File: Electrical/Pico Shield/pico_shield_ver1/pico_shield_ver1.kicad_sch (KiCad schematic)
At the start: 54 parts, among them J1 644752-2, J10 B2B-PH-K-S_LF__SN_, J11 B2B-PH-K-S_LF__SN_, J12 B2B-PH-K-S_LF__SN_, J13 B2B-PH-K-S_LF__SN_, J14 B2B-PH-K-S_LF__SN_, J2 Step_connector, J3 B5B-XH-A_LF__SN_, J4 644752-2, J5 Step_connector, J6 B5B-XH-A_LF__SN_, J7 B2B-PH-K-S_LF__SN_, J8 B2B-PH-K-S_LF__SN_, J9 B2B-PH-K-S_LF__SN_, U1 XC6230A001QR-G, U2 Si1442DH, U3 ULN2003A, U4 ULN2003A, U5 pico_shield, U6 CD4051B, U7 LM358

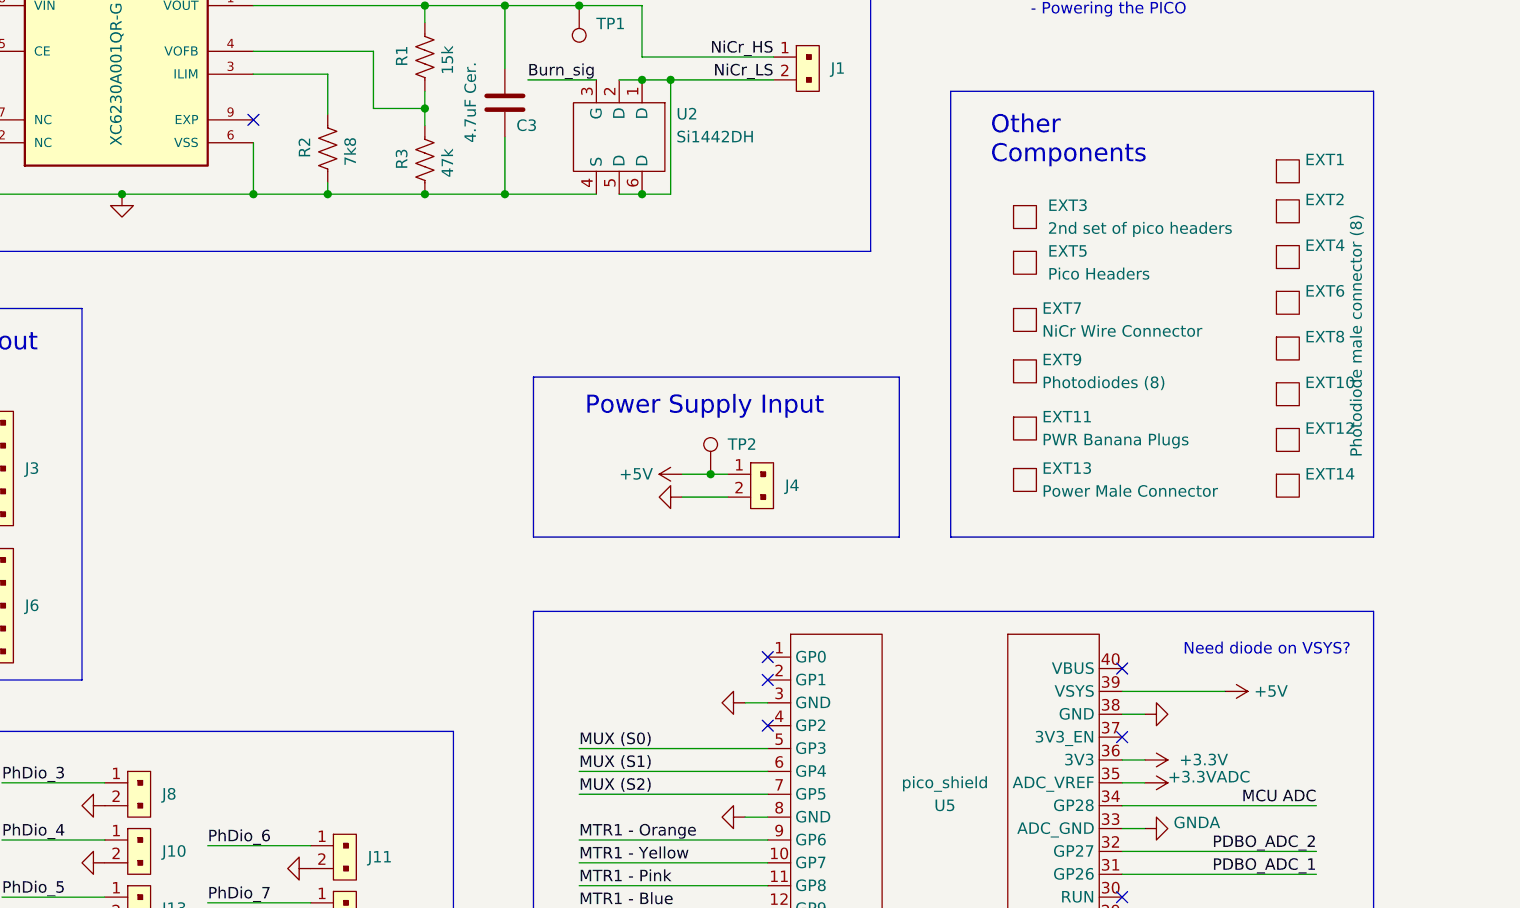
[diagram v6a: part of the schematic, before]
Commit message: Added Custom Symbols and README
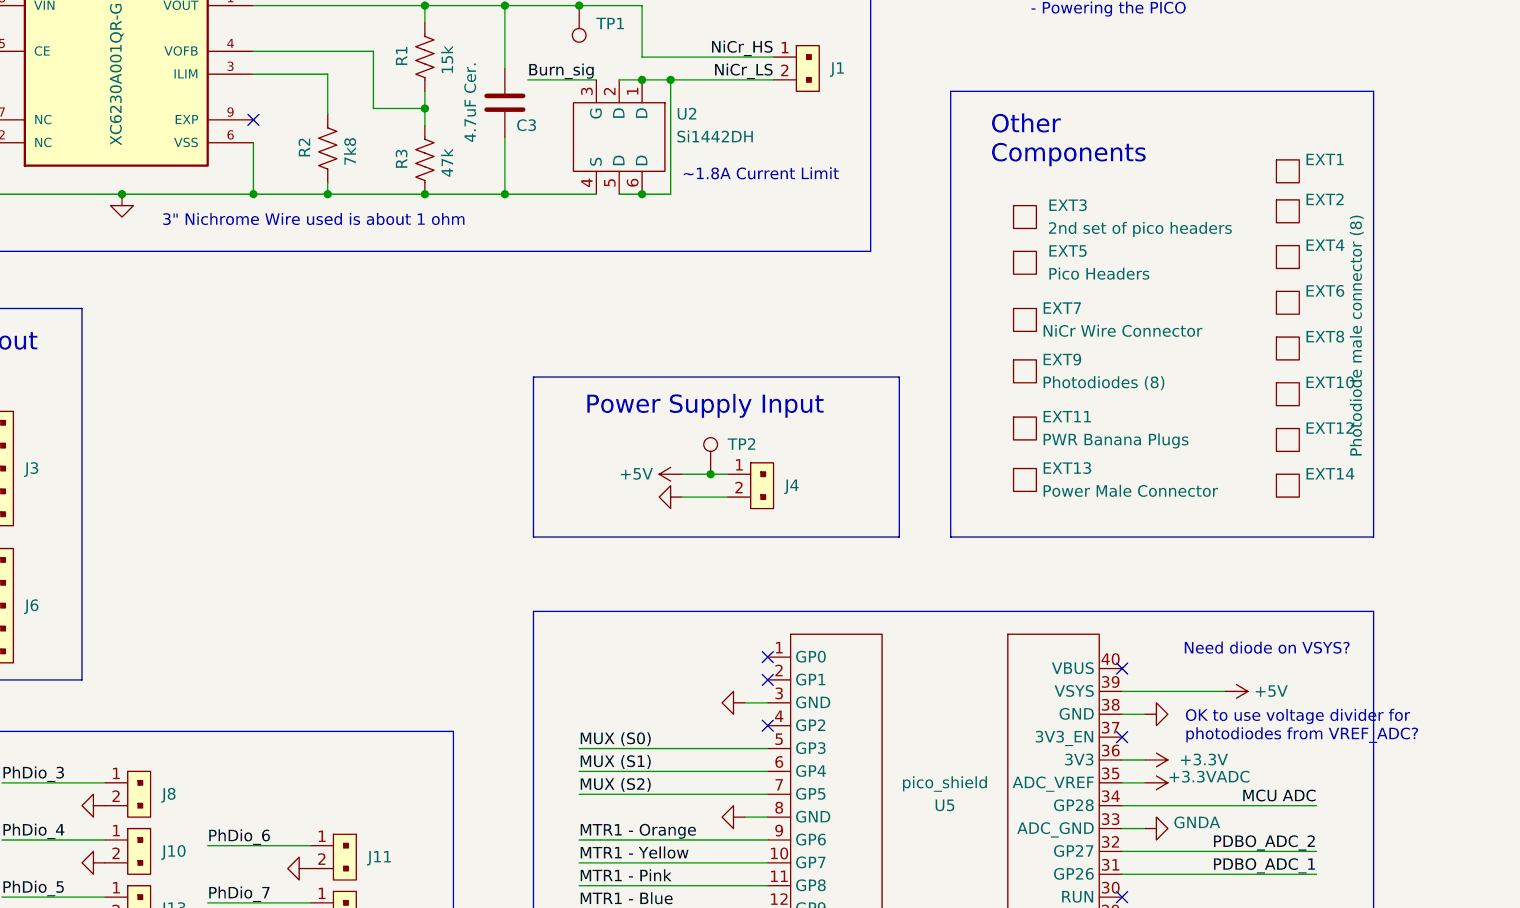
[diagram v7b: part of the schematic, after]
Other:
- note added: "3" Nichrome Wire used is about 1 ohm"
- note added: "OK to use voltage divider for photodiodes from VREF_ADC?"
- note added: "~1.8A Current Limit"
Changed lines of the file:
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@@
     (effects (font (size 2 2)) (justify left bottom))
+  )
+  (text "~1.8A Current Limit" (at 197.485 49.53 0)
+    (effects (font (size 1.27 1.27)) (justify left bottom))
+  )
+  (text "3\" Nichrome Wire used is about 1 ohm" (at 139.7 54.61 0)
+    (effects (font (size 1.27 1.27)) (justify left bottom))
   )
   (text "NiChrome Wire Burner\n" (at 179.07 26.67 0)
@@
   (text "Need diode on VSYS?" (at 271.78 102.235 180)
     (effects (font (size 1.27 1.27)) (justify right bottom))
+  )
+  (text "OK to use voltage divider for \nphotodiodes from VREF_ADC?"
+    (at 253.365 111.76 0)
+    (effects (font (size 1.27 1.27)) (justify left bottom))
   )
   (text "Step Motor Drivers" (at 53.975 33.02 0)
@@
       (effects (font (size 1.524 1.524)) (justify left) hide)
     )
-    (property "Digi-Key_PN" "455-2270-ND" (id 5) (at 63.5 93.98 0)
+    (property "Digi-Key_PN" "455-2270-ND" (id 6) (at 63.5 93.98 0)
       (effects (font (size 1.524 1.524)) (justify left) hide)
     )
@@
       (effects (font (size 1.524 1.524)) (justify left) hide)
     )
-    (property "Digi-Key_PN" "455-2270-ND" (id 5) (at 63.5 52.07 0)
-      (effects (font (size 1.524 1.524)) (justify left) hide)
-    )
+    (property "Digi-Key_PN" "455-2270-ND" (id 6) (at 63.5 52.07 0)
+      (effects (font (size 1.524 1.524)) (justify left) hide)
+    )
